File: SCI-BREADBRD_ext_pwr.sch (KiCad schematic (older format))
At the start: 8 parts

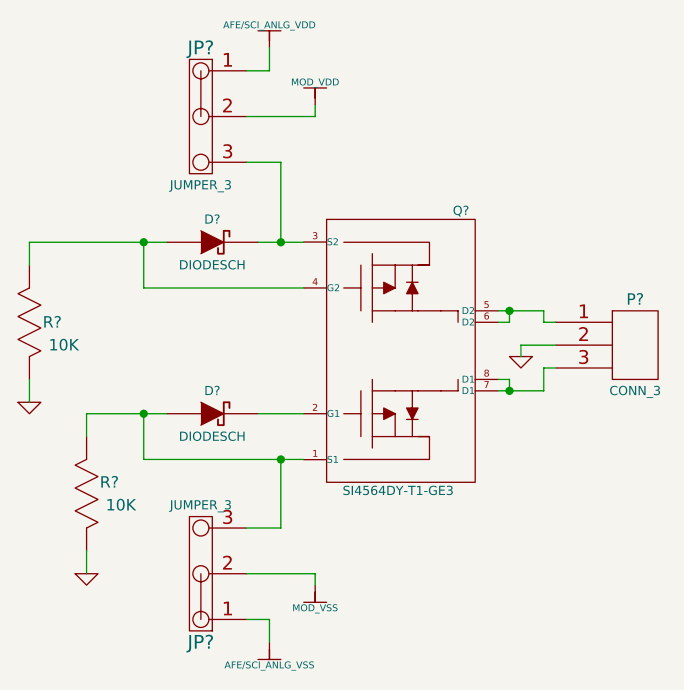
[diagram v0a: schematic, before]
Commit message: Fixed the footprint properties of various parts throughout the schematic to make sure they are all point to valid footprints.
Added SCI-BREADBRD.cmp to specify which footprints should be used for
each part.

Added netlists to the .gitignore as those can be generated easily in
eeschema.
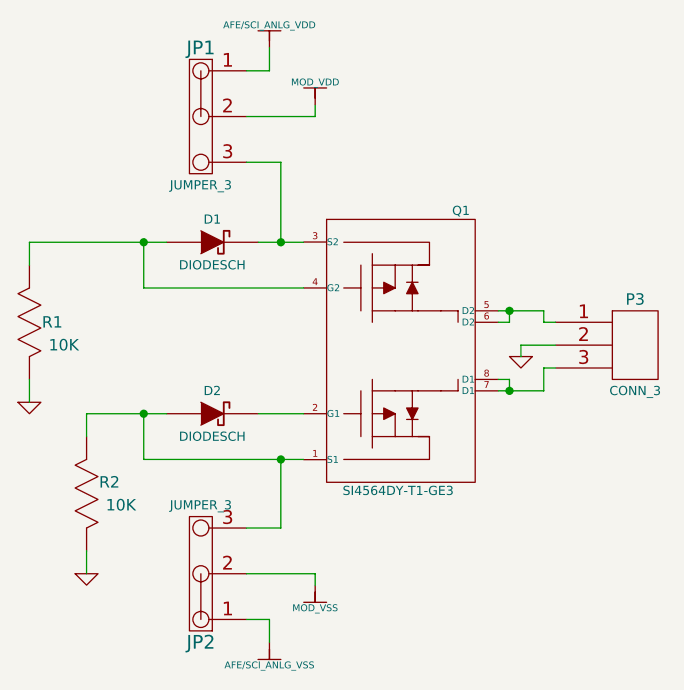
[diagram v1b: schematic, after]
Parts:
- JP1, JP2: renamed from JP?; footprint PIN_ARRAY_1x3 -> PIN_ARRAY_3X1
- R1, R2: renamed from R?; footprint SM0402 -> 0402
- gave numbers to parts that had none: 4
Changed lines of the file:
@@
-EESchema Schematic File Version 2  date Fri 27 Apr 2012 04:22:34 AM EDT
+EESchema Schematic File Version 2  date Fri 27 Apr 2012 08:55:37 AM EDT
 LIBS:custom_transistors
 LIBS:TI_custom
@@
 $EndDescr
 $Comp
-L SI4564DY-T1-GE3 Q?
+L SI4564DY-T1-GE3 Q1
 U 1 1 4F9A6317
 P 6300 3550
-F 0 "Q?" H 6588 4138 40  0000 C CNN
+F 0 "Q1" H 6588 4138 40  0000 C CNN
 F 1 "SI4564DY-T1-GE3" H 6313 2913 40  0000 C CNN
 F 2 "SOP_8_VISHAY" H 6300 3550 60  0001 C CNN
@@
 $EndComp
 $Comp
-L CONN_3 P?
+L CONN_3 P3
 U 1 1 4F9A6320
 P 7350 3550
-F 0 "P?" H 7350 3750 50  0000 C CNN
+F 0 "P3" H 7350 3750 50  0000 C CNN
 F 1 "CONN_3" H 7350 3350 40  0000 C CNN
 F 2 "PIN_ARRAY_1x3_TERMBLOCK" H 7350 3550 60  0001 C CNN
@@
 $EndComp
 $Comp
-L JUMPER_3 JP?
+L JUMPER_3 JP1
 U 1 1 4F9A6329
 P 5350 2350
-F 0 "JP?" H 5250 2450 60  0000 C CNN
+F 0 "JP1" H 5250 2450 60  0000 C CNN
 F 1 "JUMPER_3" H 5250 1850 40  0000 C CNN
-F 2 "PIN_ARRAY_1x3" H 5350 2350 60  0001 C CNN
+F 2 "PIN_ARRAY_3X1" H 5350 2350 60  0001 C CNN
 F 4 "3M" H 5350 2350 60  0001 C CNN "Manufacturer"
 F 5 "961103-6404-AR" H 5350 2350 60  0001 C CNN "Part Number"
@@
 $EndComp
 $Comp
-L JUMPER_3 JP?
+L JUMPER_3 JP2
 U 1 1 4F9A6332
 P 5350 4750
-F 0 "JP?" H 5250 4850 60  0000 C CNN
+F 0 "JP2" H 5250 4850 60  0000 C CNN
 F 1 "JUMPER_3" H 5250 4250 40  0000 C CNN
-F 2 "PIN_ARRAY_1x3" H 5350 4750 60  0001 C CNN
+F 2 "PIN_ARRAY_3X1" H 5350 4750 60  0001 C CNN
 F 4 "3M" H 5350 4750 60  0001 C CNN "Manufacturer"
 F 5 "961103-6404-AR" H 5350 4750 60  0001 C CNN "Part Number"
@@
 $EndComp
 $Comp
-L GND #PWR?
+L GND #PWR07
 U 1 1 4F9A6338
 P 6850 3600
-F 0 "#PWR?" H 6850 3600 30  0001 C CNN
+F 0 "#PWR07" H 6850 3600 30  0001 C CNN
 F 1 "GND" H 6850 3530 30  0001 C CNN
 	1    6850 3600
@@
 $EndComp
 $Comp
-L R_US R?
+L R_US R2
 U 1 1 4F9A6341
 P 4950 4200
-F 0 "R?" V 5000 4100 50  0000 C CNN
+F 0 "R2" V 5000 4100 50  0000 C CNN
 F 1 "10K" V 4900 4050 50  0000 C CNN
-F 2 "SM0402" H 4950 4200 60  0001 C CNN
+F 2 "0402" H 4950 4200 60  0001 C CNN
 F 4 "Panasonic - ECG" H 4950 4200 60  0001 C CNN "Manufacturer"
 F 5 "ERJ-2GEJ103X" H 4950 4200 60  0001 C CNN "Part Number"
@@
 $EndComp
 $Comp
-L R_US R?
+L R_US R1
 U 1 1 4F9A634A
 P 4700 3450
-F 0 "R?" V 4700 3350 50  0000 C CNN
+F 0 "R1" V 4700 3350 50  0000 C CNN
 F 1 "10K" V 4600 3300 50  0000 C CNN
-F 2 "SM0402" H 4700 3450 60  0001 C CNN
+F 2 "0402" H 4700 3450 60  0001 C CNN
 F 4 "Panasonic - ECG" H 4700 3450 60  0001 C CNN "Manufacturer"
 F 5 "ERJ-2GEJ103X" H 4700 3450 60  0001 C CNN "Part Number"
@@
 $EndComp
 $Comp
-L DIODESCH D?
+L DIODESCH D1
 U 1 1 4F9A6353
 P 5500 3100
-F 0 "D?" H 5500 3200 40  0000 C CNN
+F 0 "D1" H 5500 3200 40  0000 C CNN
 F 1 "DIODESCH" H 5500 3000 40  0000 C CNN
 F 2 "SOT_23_ON" H 5500 3100 60  0001 C CNN
@@
 $EndComp
 $Comp
-L DIODESCH D?
+L DIODESCH D2
 U 1 1 4F9A635C
 P 5500 3850
-F 0 "D?" H 5500 3950 40  0000 C CNN
+F 0 "D2" H 5500 3950 40  0000 C CNN
 F 1 "DIODESCH" H 5500 3750 40  0000 C CNN
 F 2 "SOT_23_ON" H 5500 3850 60  0001 C CNN
@@
 $EndComp
 $Comp
-L GND #PWR?
+L GND #PWR08
 U 1 1 4F9A6362
 P 4700 3800
-F 0 "#PWR?" H 4700 3800 30  0001 C CNN
+F 0 "#PWR08" H 4700 3800 30  0001 C CNN
 F 1 "GND" H 4700 3730 30  0001 C CNN
 	1    4700 3800
@@
 $EndComp
 $Comp
-L GND #PWR?
+L GND #PWR09
 U 1 1 4F9A6368
 P 4950 4550
-F 0 "#PWR?" H 4950 4550 30  0001 C CNN
+F 0 "#PWR09" H 4950 4550 30  0001 C CNN
 F 1 "GND" H 4950 4480 30  0001 C CNN
 	1    4950 4550
@@
 $EndComp
 $Comp
-L AFE/SCI_ANLG_VDD #PWR?
+L AFE/SCI_ANLG_VDD #PWR010
 U 1 1 4F9A636E
 P 5750 2250
-F 0 "#PWR?" H 5750 2350 30  0001 C CNN
+F 0 "#PWR010" H 5750 2350 30  0001 C CNN
 F 1 "AFE/SCI_ANLG_VDD" H 5750 2350 30  0000 C CNN
 	1    5750 2250
@@
 $EndComp
 $Comp
-L AFE/SCI_ANLG_VSS #PWR?
+L AFE/SCI_ANLG_VSS #PWR011
 U 1 1 4F9A6374
 P 5750 4850
-F 0 "#PWR?" H 5750 4750 30  0001 C CNN
+F 0 "#PWR011" H 5750 4750 30  0001 C CNN
 F 1 "AFE/SCI_ANLG_VSS" H 5750 4750 30  0000 C CNN
 	1    5750 4850
@@
 $EndComp
 $Comp
-L MOD_VSS #PWR?
+L MOD_VSS #PWR012
 U 1 1 4F9A637A
 P 5950 4600
-F 0 "#PWR?" H 5950 4500 30  0001 C CNN
+F 0 "#PWR012" H 5950 4500 30  0001 C CNN
 F 1 "MOD_VSS" H 5950 4500 30  0000 C CNN
 	1    5950 4600
@@
 $EndComp
 $Comp
-L MOD_VDD #PWR?
+L MOD_VDD #PWR013
 U 1 1 4F9A6380
 P 5950 2500
-F 0 "#PWR?" H 5950 2600 30  0001 C CNN
+F 0 "#PWR013" H 5950 2600 30  0001 C CNN
 F 1 "MOD_VDD" H 5950 2600 30  0000 C CNN
 	1    5950 2500
